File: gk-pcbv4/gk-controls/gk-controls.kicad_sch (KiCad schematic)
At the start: 40 parts, among them J1 Conn_01x20, U1 PCAL6416APW, U2 ULN2003A

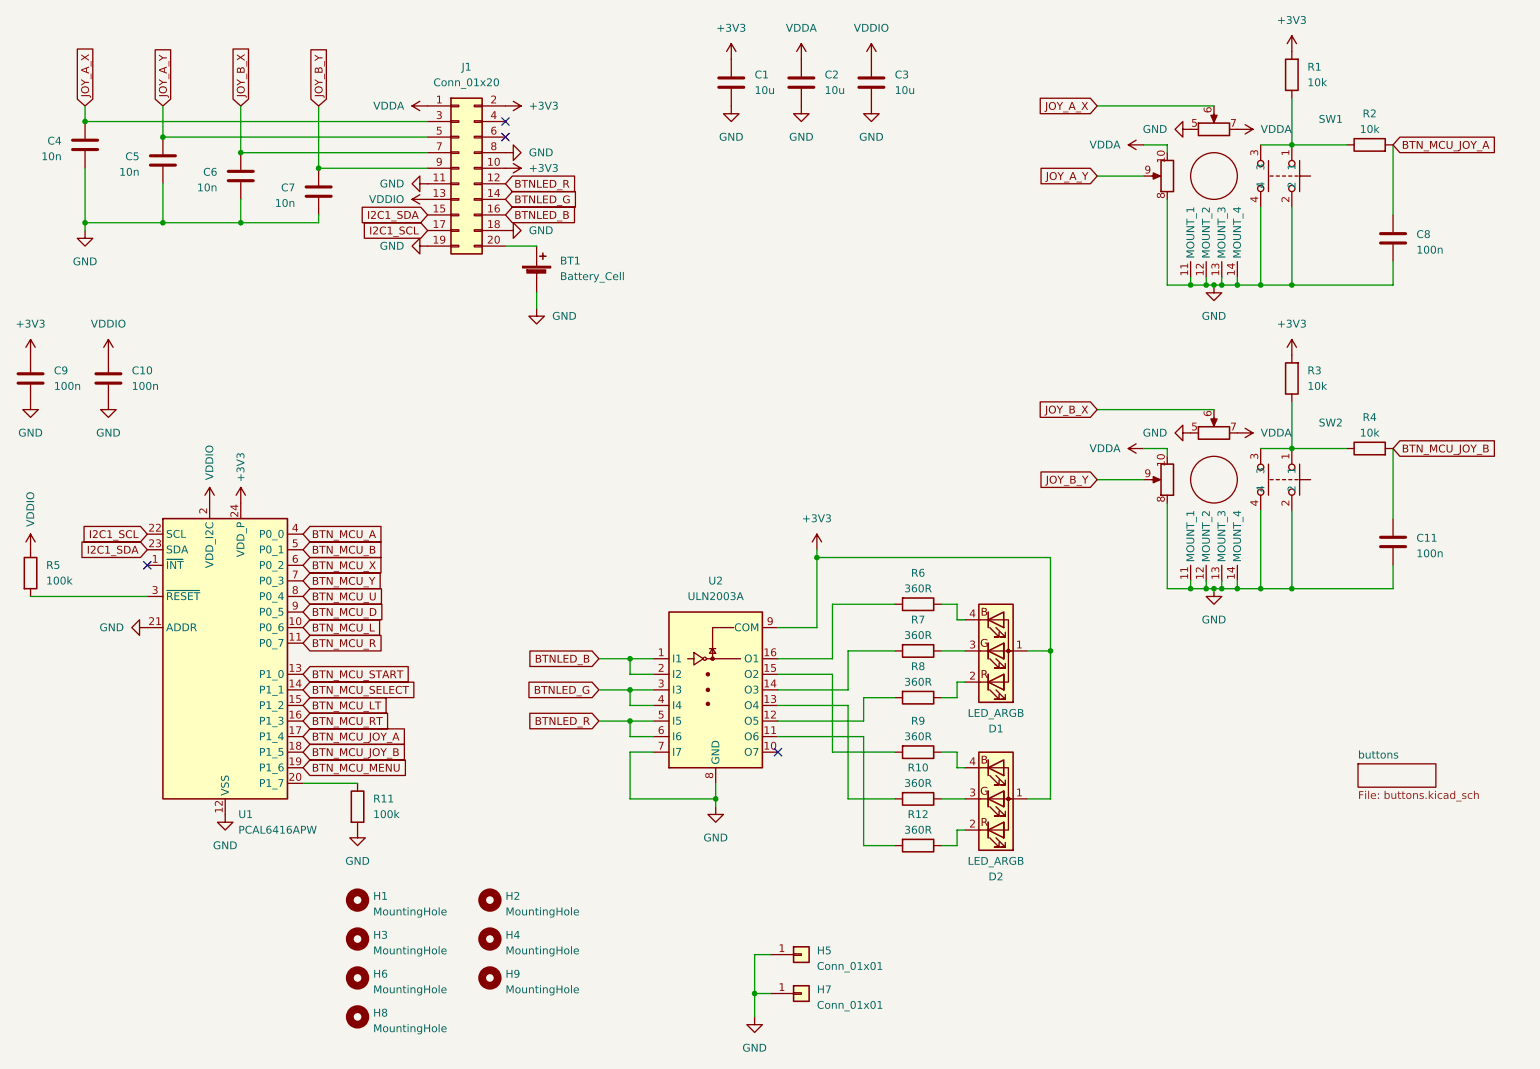
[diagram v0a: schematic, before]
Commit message: add v3 control board and trigger daughterboard
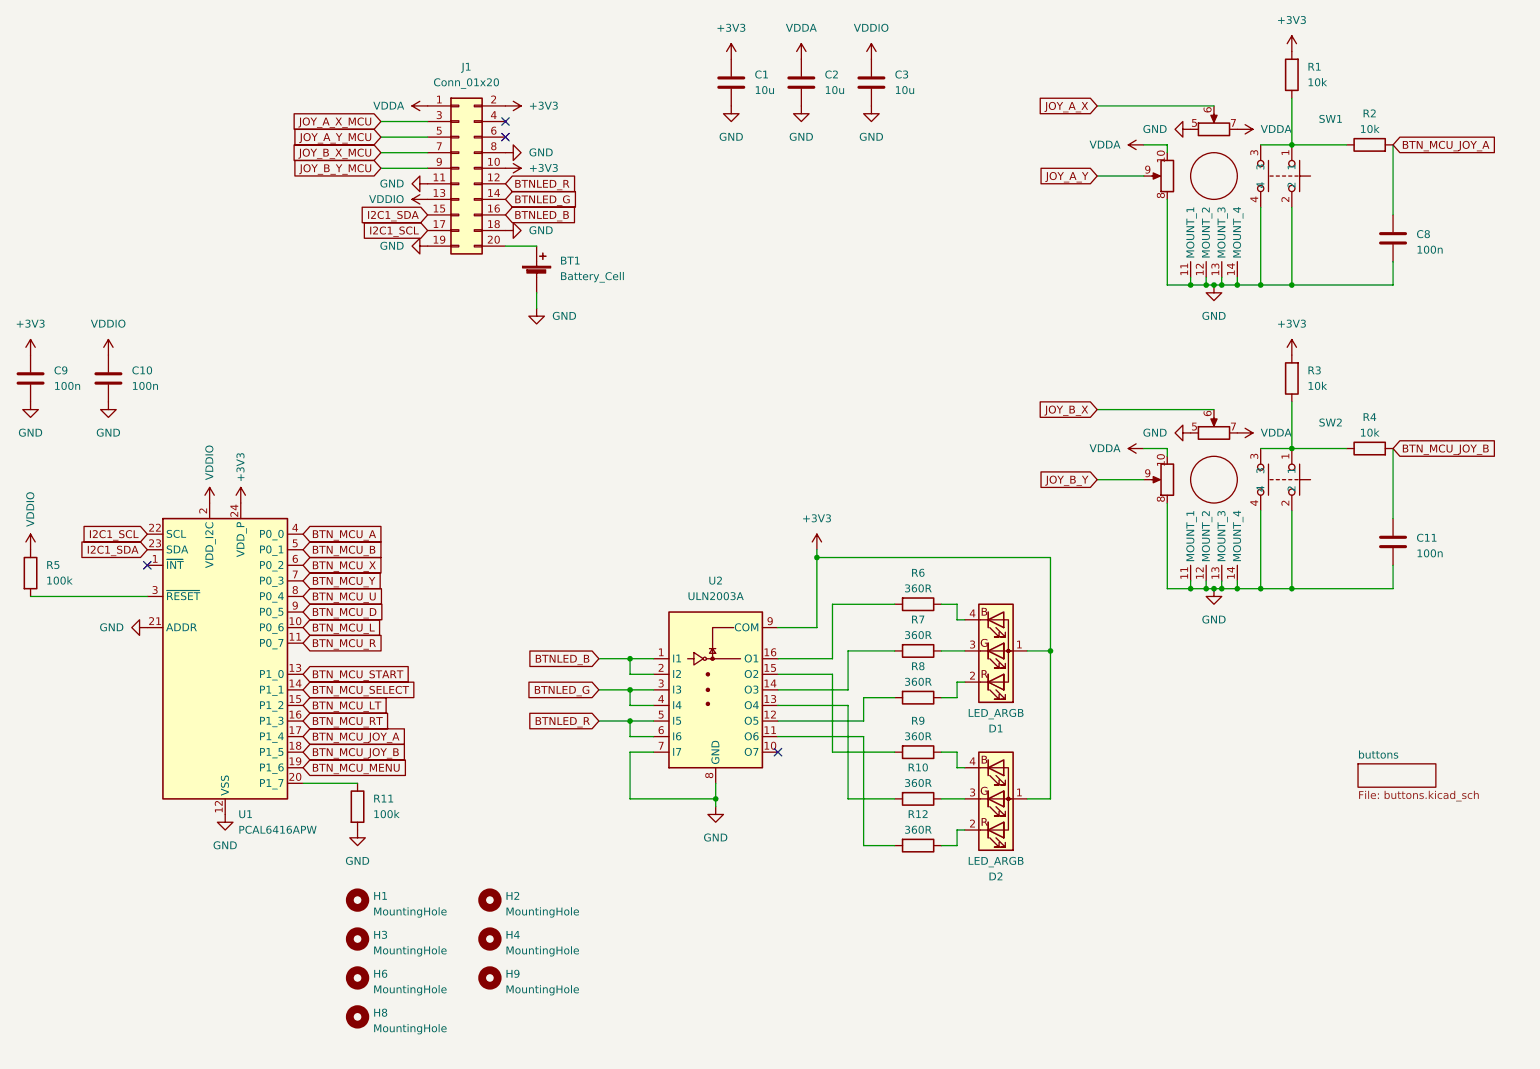
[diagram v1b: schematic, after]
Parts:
- removed C4, C5, C6, C7: 10n, Capacitor_SMD:C_0603_1608Metric, symbol Device:C
- removed H5, H7: Conn_01x01, Connector_PinHeader_2.54mm:PinHeader_1x01_P2.54mm_Vertical, symbol Connector_Generic:Conn_01x01
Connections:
- net JOY_A_X: no longer J1.3 (Pin_3)
- net JOY_A_Y: no longer J1.5 (Pin_5)
- net JOY_B_X: no longer J1.7 (Pin_7)
- net JOY_B_Y: no longer J1.9 (Pin_9)
- new net JOY_A_X_MCU: J1.3 (Pin_3)
- new net JOY_A_Y_MCU: J1.5 (Pin_5)
- new net JOY_B_X_MCU: J1.7 (Pin_7)
- new net JOY_B_Y_MCU: J1.9 (Pin_9)
